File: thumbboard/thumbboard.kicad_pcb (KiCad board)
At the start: 2 copper layers, 86 x 52 mm, 12 parts, among them J1 Conn_01x05_MountingPin, J2 Conn_01x05_MountingPin, SW1 SW_Push, SW2 SW_Push, SW3 SW_Push, SW4 SW_Push, T1 Tab, T2 Tab, T3 Tab, T4 Tab

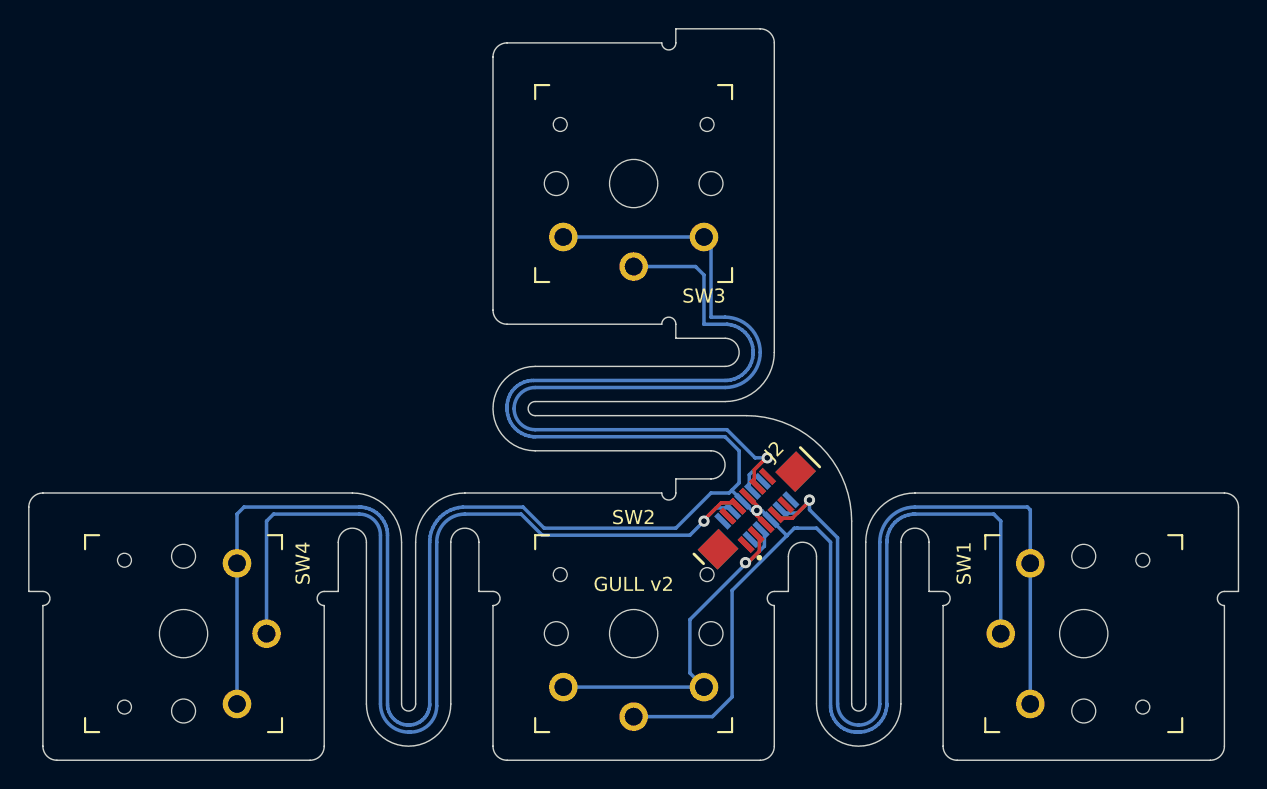
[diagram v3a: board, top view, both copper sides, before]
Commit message: Move silkscreen text to be less noticeable in final kb
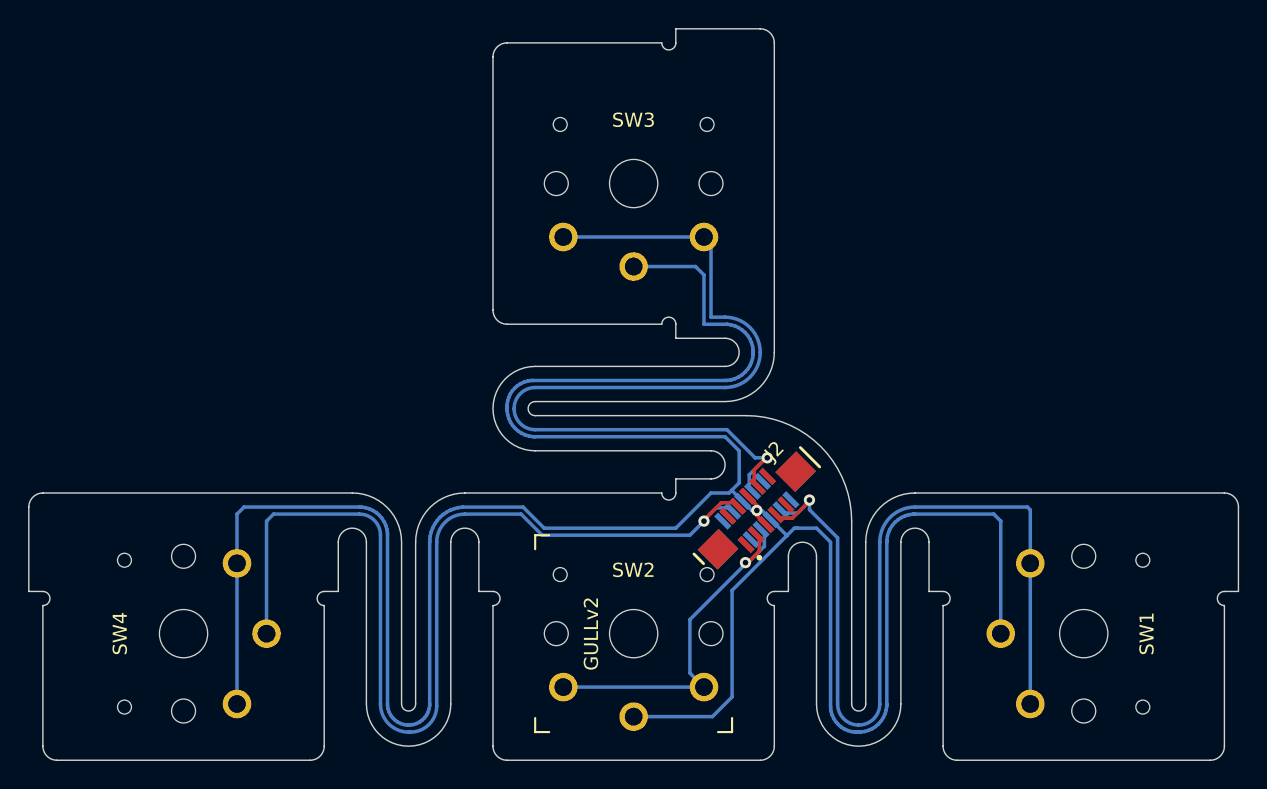
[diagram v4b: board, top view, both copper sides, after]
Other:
- board text added: "GULLv2"
- board text removed: "GULL v2"
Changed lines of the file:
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@@
     (property "ki_keywords" "switch normally-open pushbutton push-button")
     (attr through_hole)
-    (fp_text reference "SW1" (at -5 8.5 -90) (layer "F.SilkS")
+    (fp_text reference "SW1" (at 0 -4.5 -90) (layer "F.SilkS")
         (effects (font (size 1 1) (thickness 0.15)))
     )
@@
         (effects (font (size 1 1) (thickness 0.15)))
     )
-    (fp_text user "${REFERENCE}" (at -5 8.5 -90) (layer "B.SilkS")
+    (fp_text user "${REFERENCE}" (at 0 -4.5 -90) (layer "B.SilkS")
+        (effects (font (size 1 1) (thickness 0.15)) (justify mirror))
+    )
+    (fp_text user "${REFERENCE}" (at 0 0 -90) (layer "B.Fab")
         (effects (font (size 1 1) (thickness 0.15)) (justify mirror))
     )
@@
         (effects (font (size 1 1) (thickness 0.15)) (justify mirror))
     )
-    (fp_text user "${REFERENCE}" (at 0 0 -90) (layer "B.Fab")
-        (effects (font (size 1 1) (thickness 0.15)) (justify mirror))
-    )
     (fp_text user "${REFERENCE}" (at 0 0 -90) (layer "F.Fab")
         (effects (font (size 1 1) (thickness 0.15)))
     )
-    (fp_line (start -7 -7) (end -6 -7)
-      (stroke (width 0.15) (type solid)) (layer "B.SilkS"))
-    (fp_line (start -7 -6) (end -7 -7)
-      (stroke (width 0.15) (type solid)) (layer "B.SilkS"))
-    (fp_line (start -7 7) (end -7 6)
-      (stroke (width 0.15) (type solid)) (layer "B.SilkS"))
-    (fp_line (start -6 7) (end -7 7)
-      (stroke (width 0.15) (type solid)) (layer "B.SilkS"))
-    (fp_line (start 6 -7) (end 7 -7)
-      (stroke (width 0.15) (type solid)) (layer "B.SilkS"))
-    (fp_line (start 7 -7) (end 7 -6)
-      (stroke (width 0.15) (type solid)) (layer "B.SilkS"))
-    (fp_line (start 7 6) (end 7 7)
-      (stroke (width 0.15) (type solid)) (layer "B.SilkS"))
-    (fp_line (start 7 7) (end 6 7)
-      (stroke (width 0.15) (type solid)) (layer "B.SilkS"))
-    (fp_line (start -7 -7) (end -6 -7)
-      (stroke (width 0.15) (type solid)) (layer "F.SilkS"))
-    (fp_line (start -7 -6) (end -7 -7)
-      (stroke (width 0.15) (type solid)) (layer "F.SilkS"))
-    (fp_line (start -7 7) (end -7 6)
-      (stroke (width 0.15) (type solid)) (layer "F.SilkS"))
-    (fp_line (start -6 7) (end -7 7)
-      (stroke (width 0.15) (type solid)) (layer "F.SilkS"))
-    (fp_line (start 6 -7) (end 7 -7)
-      (stroke (width 0.15) (type solid)) (layer "F.SilkS"))
-    (fp_line (start 7 -7) (end 7 -6)
-      (stroke (width 0.15) (type solid)) (layer "F.SilkS"))
-    (fp_line (start 7 6) (end 7 7)
-      (stroke (width 0.15) (type solid)) (layer "F.SilkS"))
-    (fp_line (start 7 7) (end 6 7)
-      (stroke (width 0.15) (type solid)) (layer "F.SilkS"))
     (fp_line (start -6.9 6.9) (end -6.9 -6.9)
       (stroke (width 0.15) (type solid)) (layer "Eco2.User"))
@@
     (property "ki_keywords" "switch normally-open pushbutton push-button")
     (attr through_hole)
-    (fp_text reference "SW4" (at 5 8.5 90) (layer "F.SilkS")
+    (fp_text reference "SW4" (at 0 -4.5 90) (layer "F.SilkS")
         (effects (font (size 1 1) (thickness 0.15)))
     )
@@
         (effects (font (size 1 1) (thickness 0.15)))
     )
-    (fp_text user "${REFERENCE}" (at 5 8.5 90) (layer "B.SilkS")
+    (fp_text user "${REFERENCE}" (at 0 -4.5 90) (layer "B.SilkS")
         (effects (font (size 1 1) (thickness 0.15)) (justify mirror))
     )
@@
         (effects (font (size 1 1) (thickness 0.15)))
     )
-    (fp_line (start -7 -7) (end -6 -7)
-      (stroke (width 0.15) (type solid)) (layer "B.SilkS"))
-    (fp_line (start -7 -6) (end -7 -7)
-      (stroke (width 0.15) (type solid)) (layer "B.SilkS"))
-    (fp_line (start -7 7) (end -7 6)
-      (stroke (width 0.15) (type solid)) (layer "B.SilkS"))
-    (fp_line (start -6 7) (end -7 7)
-      (stroke (width 0.15) (type solid)) (layer "B.SilkS"))
-    (fp_line (start 6 -7) (end 7 -7)
-      (stroke (width 0.15) (type solid)) (layer "B.SilkS"))
-    (fp_line (start 7 -7) (end 7 -6)
-      (stroke (width 0.15) (type solid)) (layer "B.SilkS"))
-    (fp_line (start 7 6) (end 7 7)
-      (stroke (width 0.15) (type solid)) (layer "B.SilkS"))
-    (fp_line (start 7 7) (end 6 7)
-      (stroke (width 0.15) (type solid)) (layer "B.SilkS"))
-    (fp_line (start -7 -7) (end -6 -7)
-      (stroke (width 0.15) (type solid)) (layer "F.SilkS"))
-    (fp_line (start -7 -6) (end -7 -7)
-      (stroke (width 0.15) (type solid)) (layer "F.SilkS"))
-    (fp_line (start -7 7) (end -7 6)
-      (stroke (width 0.15) (type solid)) (layer "F.SilkS"))
-    (fp_line (start -6 7) (end -7 7)
-      (stroke (width 0.15) (type solid)) (layer "F.SilkS"))
-    (fp_line (start 6 -7) (end 7 -7)
-      (stroke (width 0.15) (type solid)) (layer "F.SilkS"))
-    (fp_line (start 7 -7) (end 7 -6)
-      (stroke (width 0.15) (type solid)) (layer "F.SilkS"))
-    (fp_line (start 7 6) (end 7 7)
-      (stroke (width 0.15) (type solid)) (layer "F.SilkS"))
-    (fp_line (start 7 7) (end 6 7)
-      (stroke (width 0.15) (type solid)) (layer "F.SilkS"))
     (fp_line (start -6.9 6.9) (end -6.9 -6.9)
       (stroke (width 0.15) (type solid)) (layer "Eco2.User"))
@@
     (property "ki_keywords" "switch normally-open pushbutton push-button")
     (attr through_hole)
-    (fp_text reference "SW3" (at 5 8) (layer "F.SilkS")
+    (fp_text reference "SW3" (at 0 -4.5) (layer "F.SilkS")
         (effects (font (size 1 1) (thickness 0.15)))
     )
@@
         (effects (font (size 1 1) (thickness 0.15)))
     )
-    (fp_text user "${REFERENCE}" (at 5 8) (layer "B.SilkS")
+    (fp_text user "${REFERENCE}" (at 0 -4.5) (layer "B.SilkS")
+        (effects (font (size 1 1) (thickness 0.15)) (justify mirror))
+    )
+    (fp_text user "${REFERENCE}" (at 0 0) (layer "B.Fab")
         (effects (font (size 1 1) (thickness 0.15)) (justify mirror))
     )
@@
         (effects (font (size 1 1) (thickness 0.15)) (justify mirror))
     )
-    (fp_text user "${REFERENCE}" (at 0 0) (layer "B.Fab")
-        (effects (font (size 1 1) (thickness 0.15)) (justify mirror))
-    )
     (fp_text user "${REFERENCE}" (at 0 0) (layer "F.Fab")
         (effects (font (size 1 1) (thickness 0.15)))
     )
-    (fp_line (start -7 -7) (end -6 -7)
-      (stroke (width 0.15) (type solid)) (layer "B.SilkS"))
-    (fp_line (start -7 -6) (end -7 -7)
-      (stroke (width 0.15) (type solid)) (layer "B.SilkS"))
-    (fp_line (start -7 7) (end -7 6)
-      (stroke (width 0.15) (type solid)) (layer "B.SilkS"))
-    (fp_line (start -6 7) (end -7 7)
-      (stroke (width 0.15) (type solid)) (layer "B.SilkS"))
-    (fp_line (start 6 -7) (end 7 -7)
-      (stroke (width 0.15) (type solid)) (layer "B.SilkS"))
-    (fp_line (start 7 -7) (end 7 -6)
-      (stroke (width 0.15) (type solid)) (layer "B.SilkS"))
-    (fp_line (start 7 6) (end 7 7)
-      (stroke (width 0.15) (type solid)) (layer "B.SilkS"))
-    (fp_line (start 7 7) (end 6 7)
-      (stroke (width 0.15) (type solid)) (layer "B.SilkS"))
-    (fp_line (start -7 -7) (end -6 -7)
-      (stroke (width 0.15) (type solid)) (layer "F.SilkS"))
-    (fp_line (start -7 -6) (end -7 -7)
-      (stroke (width 0.15) (type solid)) (layer "F.SilkS"))
-    (fp_line (start -7 7) (end -7 6)
-      (stroke (width 0.15) (type solid)) (layer "F.SilkS"))
-    (fp_line (start -6 7) (end -7 7)
-      (stroke (width 0.15) (type solid)) (layer "F.SilkS"))
-    (fp_line (start 6 -7) (end 7 -7)
-      (stroke (width 0.15) (type solid)) (layer "F.SilkS"))
-    (fp_line (start 7 -7) (end 7 -6)
-      (stroke (width 0.15) (type solid)) (layer "F.SilkS"))
-    (fp_line (start 7 6) (end 7 7)
-      (stroke (width 0.15) (type solid)) (layer "F.SilkS"))
-    (fp_line (start 7 7) (end 6 7)
-      (stroke (width 0.15) (type solid)) (layer "F.SilkS"))
     (fp_line (start -6.9 6.9) (end -6.9 -6.9)
       (stroke (width 0.15) (type solid)) (layer "Eco2.User"))
@@
     (property "ki_keywords" "switch normally-open pushbutton push-button")
     (attr through_hole)
-    (fp_text reference "SW2" (at 0 -8.255) (layer "F.SilkS")
+    (fp_text reference "SW2" (at 0 -4.5) (layer "F.SilkS")
         (effects (font (size 1 1) (thickness 0.15)))
     )
@@
         (effects (font (size 1 1) (thickness 0.15)))
     )
-    (fp_text user "${REFERENCE}" (at 0 -8.255) (layer "B.SilkS")
+    (fp_text user "${REFERENCE}" (at 0 -4.5) (layer "B.SilkS")
         (effects (font (size 1 1) (thickness 0.15)) (justify mirror))
     )
@@
   (gr_arc (start 166.5 114.5) (mid 163.5 117.5) (end 160.5 114.5)
     (stroke (width 0.1) (type default)) (layer "Edge.Cuts"))
-  (gr_text "GULL v2" (at 147.5 106) (layer "F.SilkS")
+  (gr_text "GULLv2" (at 144.5 109.5 90) (layer "B.SilkS")
+    (effects (font (size 1 1) (thickness 0.15)) (justify mirror))
+  )
+  (gr_text "GULLv2" (at 144.5 109.5 90) (layer "F.SilkS")
     (effects (font (size 1 1) (thickness 0.15)))
   )
